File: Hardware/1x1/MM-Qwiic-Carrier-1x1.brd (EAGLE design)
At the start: 80 x 34.3 mm, 63 parts, among them J15 MICROMOD-2222-C, J2 QWIIC_RIGHT_ANGLE, U1 MCP73831, U5 AP7361C-33FGEUDFN-8

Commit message: Remove production files. Design review changes
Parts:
- removed H6, H7, H8, H9: STAND-OFF-REFLOW2.5MM_TALL, SparkFun-Hardware:STAND-OFF-REFLOW-M2.5
- removed JP1: JUMPER-SMT_2_NC_TRACE_SILK, SparkFun-Jumpers:SMT-JUMPER_2_NC_TRACE_SILK
- added D5: 3A/10V/280mV, SparkFun-DiscreteSemi:SOD-323
- added J4: (no value), SparkFun-Connectors:1X02_NO_SILK
- added J5: Vertical Qwiic Connector, SparkFun-Connectors:JST04_1MM_VERT
- added J6: (no value), SparkFun-Connectors:1X08_NO_SILK
- added TP1, TP2: TEST-POINT3X5, SparkFun-Connectors:PAD.03X.05
- U$5: value (none) -> QWIIC_BOARD_OUTLINESTANDOFF; device output:#VIN#0 -> SparkFun-Boards:QWIIC_BOARD_MOUNT_SMD_STANDOFFS
- moved U$5 47.9 mm to (62.2, 17.8), flipped to the top
- moved U$3 41.5 mm to (91.8, 10.7)
- moved LOGO2 27.9 mm to (33.4, 3.11)
- moved J2 27.9 mm to (38.1, 5.08)
- moved U$4 17.4 mm to (5.84, 31.8)
- moved D4 17.3 mm to (11.4, 31.8)
- moved JP4 15.1 mm to (15.2, 33.7)
- moved R11 15.1 mm to (15.2, 33.7)
- moved U$6 15.1 mm to (21.0, 33.5)
- moved R4 11.9 mm to (15.0, 29.2)
- moved D2 11.3 mm to (11.4, 33.7), turned to 180 degrees
- moved U$19 10.5 mm to (15.9, 0.76), turned to 90 degrees
- moved U$2 10.4 mm to (6.99, 0.51), turned to 90 degrees
- moved C3 8.38 mm to (13.0, 29.2)
- moved J3 8.13 mm to (3.81, 25.4), turned to 90 degrees
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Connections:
- removed net 5V: C4.1, D3.C, D4.A, JP1.2, U1.4
- removed net I2C_SCL: J15.14, J2.4
- removed net I2C_SDA: J15.12, J2.3
- removed net N$5: C3.1, D3.A, J3.2, U1.3
- new net D0: J15.10, J6.3
- new net D1: J15.18, J6.4
- new net I2C_!INT!: J15.16, J6.2
- new net SCL: J15.14, J2.4, J5.4, TP2.P$1
- new net SDA: J15.12, J2.3, J5.3, TP1.P$1
- new net SPI_!CS!: J15.55, J6.8
- new net SPI_CIPO: J15.61, J6.5
- new net SPI_COPI: J15.59, J6.6
- new net SPI_SCK: J15.57, J6.7
- new net V_BATT: C3.1, D3.A, J3.2, J4.1, U1.3
- net 3.3V: now also J5.2
- net GND: now also J4.2, J5.1, J6.1; no longer H6.1, H7.1, H8.1, H9.1
- net N$3: now also D4.C; no longer U1.1
- net N$8: now also U1.1; no longer D4.C
- net VIN: now also D3.C, D5.C; no longer JP1.1
- net V_USB: now also C4.1, D4.A, D5.A, U1.4
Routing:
- net SPI_!CS!: track 0.00 -> 34.9 mm, vias 0 -> 1
- net SPI_SCK: track 0.00 -> 32.4 mm, vias 0 -> 1
- net SPI_COPI: track 0.00 -> 29.3 mm, vias 0 -> 1
- net SDA: track 0.00 -> 28.3 mm, vias 0 -> 2
- net SCL: track 0.00 -> 27.4 mm
- net D0: track 0.00 -> 27.1 mm, vias 0 -> 2
- net D1: track 0.00 -> 27.1 mm
- net SPI_CIPO: track 0.00 -> 26.4 mm, vias 0 -> 1
- net I2C_!INT!: track 0.00 -> 26.2 mm
- net V_USB: track 18.2 -> 44.3 mm, vias 1 -> 3
- net V_BATT: track 0.00 -> 21.7 mm, vias 0 -> 1
- net I2C_SDA: track 20.7 -> 0.00 mm, vias 2 -> 0
- net I2C_SCL: track 20.0 -> 0.00 mm, vias 2 -> 0
- net N$5: track 12.7 -> 0.00 mm
- net 5V: track 12.2 -> 0.00 mm, vias 1 -> 0
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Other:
- board size 80 x 34.3 mm -> 80 x 35.6 mm
- board text added: "in"

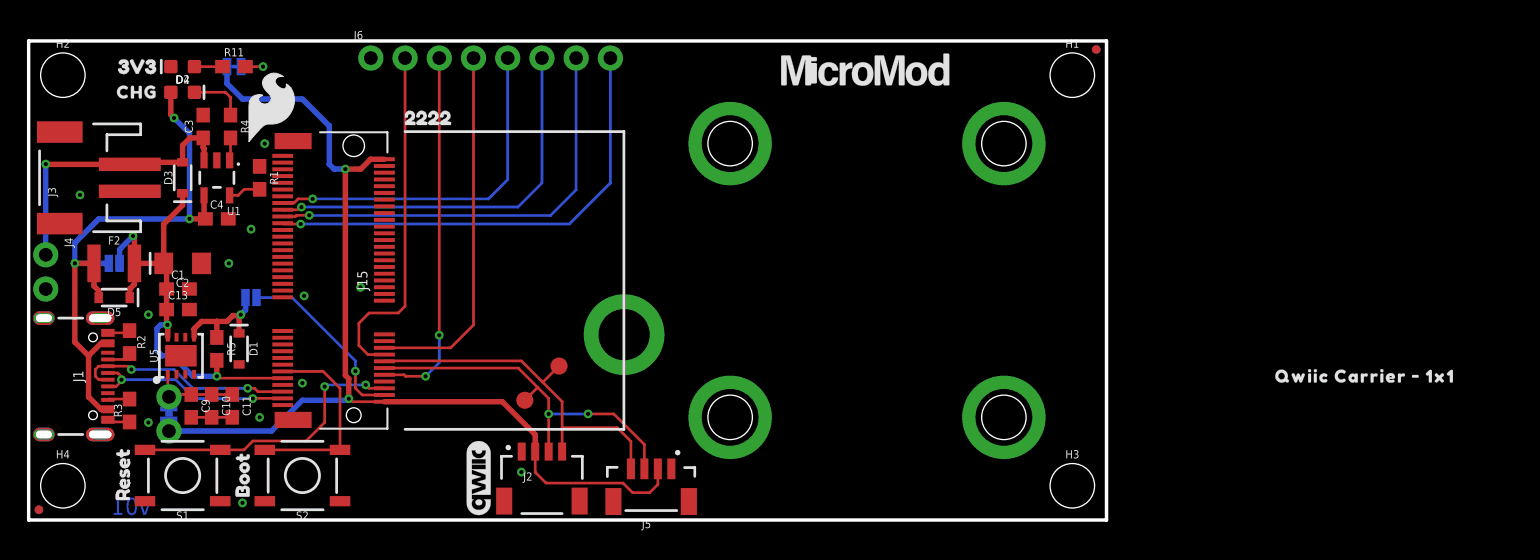
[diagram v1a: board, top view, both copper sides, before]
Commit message: Fix silk screen
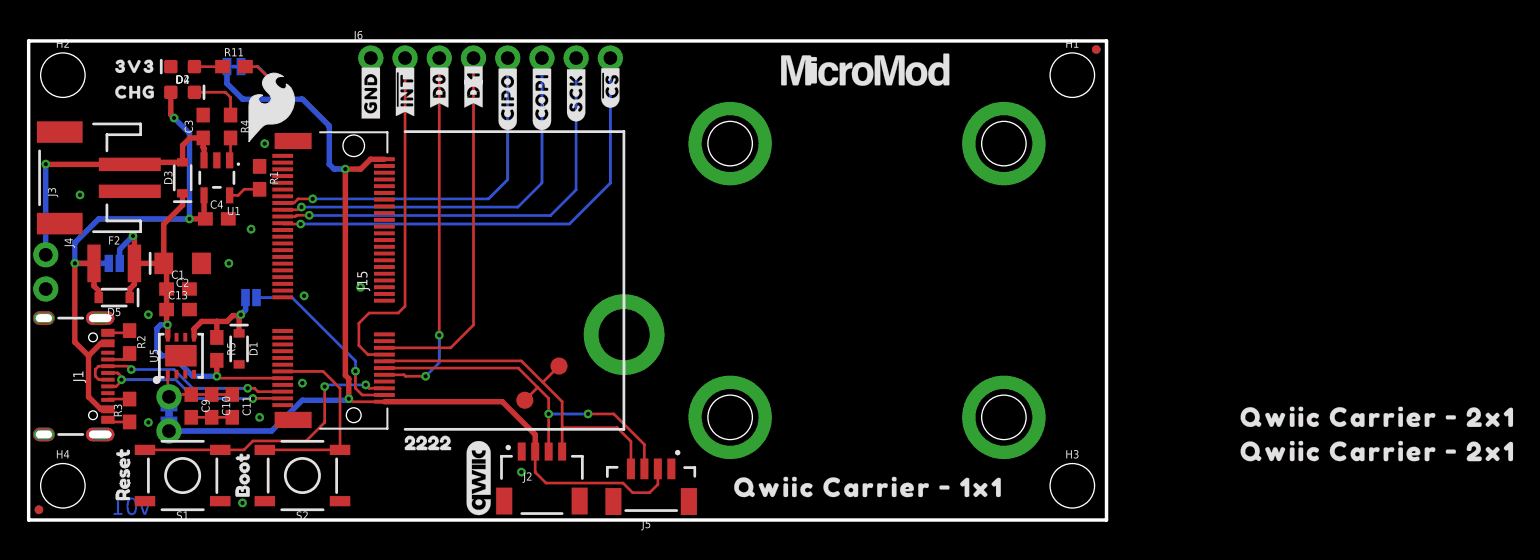
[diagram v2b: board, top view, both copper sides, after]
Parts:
- added U$10, U$13: (no value), output:QWIIC_CARRIER_#_1X10
- added U$11, U$12: (no value), output:QWIIC_CARRIER_#_2X10
- added U$14: (no value), output:#GND#0
- added U$15, U$16: (no value), output:##INT##0
- added U$17, U$18: (no value), output:#D0#0
- added U$20, U$21: (no value), output:#D#0
- added U$22, U$23: (no value), output:#CIPO#0
- added U$24, U$25: (no value), output:#COPI#0
- added U$26, U$27: (no value), output:#SCK#0
- added U$28, U$29: (no value), output:##CS##0
- added U$30, U$31: (no value), output:#1#0
- U$1: device buzzard_labels (5):3V31 -> output:#3#3V_EN#0
- U$3: device output:QWIIC_CARRIER_#_1X1_0 -> output:3V30
- U$8: device output:#VE#0 -> output:#GND#0
- moved U$3 89.1 mm to (5.71, 33.7)
- moved U$55 24.1 mm to (27.0, 5.72)
- moved U$1 19.9 mm to (15.7, 16.5), flipped to the bottom
- moved U$8 16.2 mm to (25.4, 29.5), flipped to the top, turned to 90 degrees
- moved U$68 3.81 mm to (31.8, 19.1)
- moved LOGO1 2.54 mm to (31.8, 21.6)
- moved LOGO3 1.27 mm to (31.6, 10.9)
- moved U$4 0.13 mm to (5.71, 31.8)
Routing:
- net N$4: track 2.95 -> 5.24 mm
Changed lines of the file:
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@@
 <?xml version="1.0" encoding="utf-8"?>
 <!DOCTYPE eagle SYSTEM "eagle.dtd">
-<eagle version="9.5.2">
+<eagle version="9.6.2">
 <drawing>
 <settings>
@@
 <element name="U$19" library="buzzard_labels (10)" package="BOOT2" value="" x="15.875" y="0.762" smashed="yes" rot="R90"/>
 <element name="LOGO2" library="SparkFun-Aesthetics" package="QWIIC_5.5MM" value="QWIIC_LOGO_CONNECTOR" x="33.401" y="3.1115" smashed="yes" rot="R90"/>
-<element name="LOGO3" library="SparkFun-Aesthetics" package="OSHW-LOGO-M" value="OSHW-LOGOM" x="31.623" y="9.652" smashed="yes" rot="MR0"/>
-<element name="U$55" library="buzzard_labels (9)" package="22229" value="" x="26.962" y="29.85" smashed="yes"/>
+<element name="LOGO3" library="SparkFun-Aesthetics" package="OSHW-LOGO-M" value="OSHW-LOGOM" x="31.623" y="10.922" smashed="yes" rot="MR0"/>
+<element name="U$55" library="buzzard_labels (9)" package="22229" value="" x="26.962" y="5.72" smashed="yes"/>
 <element name="H5" library="SparkFun-Hardware" package="STAND-OFF-REFLOW-M2.5" value="STAND-OFF-REFLOW2.5MM_TALL" x="44.2" y="13.76" smashed="yes">
 <attribute name="PROD_ID" value="HW-14899" x="44.2" y="13.76" size="1.778" layer="27" font="vector" ratio="15" display="off"/>
@@
 <attribute name="VALUE" x="23.495" y="17.78" size="0.762" layer="27" rot="R270" align="center"/>
 </element>
-<element name="LOGO1" library="SparkFun-Aesthetics" package="SFE_LOGO_NAME_FLAME_.2" value="SFE_LOGO_NAME_FLAME.2_INCH" x="31.75" y="19.05" smashed="yes" rot="MR0"/>
-<element name="U$1" library="buzzard_labels (5)" package="3V31" value="" x="5.715" y="33.655" smashed="yes"/>
+<element name="LOGO1" library="SparkFun-Aesthetics" package="SFE_LOGO_NAME_FLAME_.2" value="SFE_LOGO_NAME_FLAME.2_INCH" x="31.75" y="21.59" smashed="yes" rot="MR0"/>
 <element name="U$44" library="SparkFun-Aesthetics" package="SFE_LOGO_FLAME_.2" value="" x="18.034" y="30.607" smashed="yes"/>
 <element name="U$67" library="SparkFun-MicroMod" package="MICROMOD_LOGO_.5" value="" x="62.103" y="33.401" smashed="yes"/>
-<element name="U$68" library="SparkFun-MicroMod" package="MICROMOD_LOGO_.5" value="" x="31.75" y="15.24" smashed="yes" rot="MR0"/>
+<element name="U$68" library="SparkFun-MicroMod" package="MICROMOD_LOGO_.5" value="" x="31.75" y="19.05" smashed="yes" rot="MR0"/>
 <element name="J2" library="SparkFun-Connectors" package="JST04_1MM_RA" value="QWIIC_RIGHT_ANGLE" x="38.1" y="5.08" smashed="yes">
 <attribute name="NAME" x="36.703" y="2.921" size="0.6096" layer="25" font="vector" ratio="20"/>
@@
 <attribute name="VALUE" x="14.224" y="29.21" size="0.6096" layer="27" font="vector" ratio="20" rot="R270" align="top-center"/>
 </element>
-<element name="U$3" library="output" package="QWIIC_CARRIER_#_1X1_0" value="" x="91.821" y="10.668" smashed="yes"/>
-<element name="U$4" library="output" package="CHG0" value="" x="5.842" y="31.75" smashed="yes"/>
+<element name="U$4" library="output" package="CHG0" value="" x="5.715" y="31.75" smashed="yes"/>
 <element name="U$6" library="output" package="#3#3V#0" value="" x="20.955" y="33.528" smashed="yes" rot="MR0"/>
 <element name="U$7" library="output" package="#BYP#0" value="" x="11.43" y="19.05" smashed="yes" rot="MR0"/>
 <element name="U$9" library="output" package="#MEAS#0" value="" x="16.51" y="7.874" smashed="yes" rot="MR0"/>
-<element name="U$8" library="output" package="#VE#0" value="" x="15.748" y="16.51" smashed="yes" rot="MR0"/>
 <element name="TP1" library="SparkFun-Connectors" package="PAD.03X.05" value="TEST-POINT3X5" x="36.83" y="8.89" smashed="yes"/>
 <element name="TP2" library="SparkFun-Connectors" package="PAD.03X.05" value="TEST-POINT3X5" x="39.37" y="11.43" smashed="yes"/>
@@
 </element>
 <element name="U$5" library="SparkFun-Boards" package="QWIIC_BOARD_MOUNT_SMD_STANDOFFS" value="QWIIC_BOARD_OUTLINESTANDOFF" x="62.23" y="17.78" smashed="yes"/>
+<element name="U$10" library="output" package="QWIIC_CARRIER_#_1X10" value="" x="51.308" y="2.413" smashed="yes"/>
+<element name="U$11" library="output" package="QWIIC_CARRIER_#_2X10" value="" x="88.9" y="7.62" smashed="yes"/>
+<element name="U$12" library="output" package="QWIIC_CARRIER_#_2X10" value="" x="88.9" y="5.08" smashed="yes"/>
+<element name="U$13" library="output" package="QWIIC_CARRIER_#_1X10" value="" x="42.672" y="16.637" smashed="yes" rot="MR0"/>
+<element name="U$3" library="output" package="3V30" value="" x="5.715" y="33.655" smashed="yes"/>
+<element name="U$1" library="output" package="#3#3V_EN#0" value="" x="15.748" y="16.51" smashed="yes" rot="MR0"/>
+<element name="U$8" library="output" package="#GND#0" value="" x="25.4" y="29.464" smashed="yes" rot="R90"/>
+<element name="U$14" library="output" package="#GND#0" value="" x="25.4" y="29.464" smashed="yes" rot="MR90"/>
+<element name="U$15" library="output" package="##INT##0" value="" x="27.94" y="29.972" smashed="yes" rot="R90"/>
+<element name="U$16" library="output" package="##INT##0" value="" x="27.94" y="29.972" smashed="yes" rot="MR90"/>
+<element name="U$17" library="output" package="#D0#0" value="" x="30.48" y="30.607" smashed="yes" rot="R90"/>
+<element name="U$18" library="output" package="#D0#0" value="" x="30.48" y="30.607" smashed="yes" rot="MR90"/>
+<element name="U$22" library="output" package="#CIPO#0" value="" x="35.56" y="28.956" smashed="yes" rot="R90"/>
+<element name="U$23" library="output" package="#CIPO#0" value="" x="35.56" y="28.956" smashed="yes" rot="MR90"/>
+<element name="U$24" library="output" package="#COPI#0" value="" x="38.1" y="28.956" smashed="yes" rot="R90"/>
+<element name="U$25" library="output" package="#COPI#0" value="" x="38.1" y="28.956" smashed="yes" rot="MR90"/>
+<element name="U$26" library="output" package="#SCK#0" value="" x="40.64" y="29.591" smashed="yes" rot="R90"/>
+<element name="U$27" library="output" package="#SCK#0" value="" x="40.64" y="29.591" smashed="yes" rot="MR90"/>
+<element name="U$28" library="output" package="##CS##0" value="" x="43.18" y="30.607" smashed="yes" rot="R90"/>
+<element name="U$29" library="output" package="##CS##0" value="" x="43.18" y="30.607" smashed="yes" rot="MR90"/>
+<element name="U$20" library="output" package="#D#0" value="" x="33.02" y="30.607" smashed="yes" rot="R90"/>
+<element name="U$21" library="output" package="#D#0" value="" x="33.02" y="30.607" smashed="yes" rot="MR90"/>
+<element name="U$30" library="output" package="#1#0" value="" x="33.02" y="32.004" smashed="yes" rot="R90"/>
+<element name="U$31" library="output" package="#1#0" value="" x="33.02" y="32.004" smashed="yes" rot="MR90"/>
 </elements>
 <signals>
@@
 <contactref element="R11" pad="2"/>
 <contactref element="JP4" pad="1"/>
-<wire x1="16.09" y1="33.655" x2="17.399" y2="33.655" width="0.2032" layer="1"/>
-<via x="17.399" y="33.655" extent="1-16" drill="0.3048"/>
-<wire x1="17.399" y1="33.655" x2="15.7607" y2="33.655" width="0.2032" layer="16"/>
+<wire x1="17.653" y1="32.385" x2="17.653" y2="32.981" width="0.2032" layer="1"/>
+<wire x1="17.653" y1="32.981" x2="16.979" y2="33.655" width="0.2032" layer="1"/>
+<wire x1="16.09" y1="33.655" x2="16.979" y2="33.655" width="0.2032" layer="1"/>
+<via x="17.653" y="32.385" extent="1-16" drill="0.3048"/>
+<wire x1="17.653" y1="32.385" x2="17.653" y2="33.0327" width="0.2032" layer="16"/>
+<wire x1="17.653" y1="33.0327" x2="17.0307" y2="33.655" width="0.2032" layer="16"/>
+<wire x1="17.0307" y1="33.655" x2="15.7607" y2="33.655" width="0.2032" layer="16"/>
 </signal>
 <signal name="N$6">

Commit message: Checklist
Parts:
- removed U$11, U$12: (no value), output:QWIIC_CARRIER_#_2X10
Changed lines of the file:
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@@
 <?xml version="1.0" encoding="utf-8"?>
 <!DOCTYPE eagle SYSTEM "eagle.dtd">
-<eagle version="9.6.2">
+<eagle version="9.5.2">
 <drawing>
 <settings>
-<setting alwaysvectorfont="yes"/>
+<setting alwaysvectorfont="no"/>
 <setting verticaltext="up"/>
 </settings>
@@
 <layer number="37" name="tTest" color="7" fill="1" visible="no" active="yes"/>
 <layer number="38" name="bTest" color="7" fill="1" visible="no" active="yes"/>
-<layer number="39" name="tKeepout" color="4" fill="11" visible="yes" active="yes"/>
+<layer number="39" name="tKeepout" color="4" fill="11" visible="no" active="yes"/>
 <layer number="40" name="bKeepout" color="1" fill="11" visible="no" active="yes"/>
 <layer number="41" name="tRestrict" color="4" fill="10" visible="no" active="yes"/>
@@
 <text x="43.434" y="39.878" size="1.778" layer="47" font="vector" ratio="15">in</text>
 <text x="81.534" y="23.241" size="1.778" layer="47" font="vector" ratio="15" rot="R270">in</text>
+<dimension x1="2.54" y1="33.02" x2="77.47" y2="33.02" x3="40.005" y3="44.45" textsize="1.778" textratio="15" layer="47" unit="inch"/>
+<dimension x1="77.47" y1="33.02" x2="77.47" y2="2.54" x3="88.9" y3="17.78" textsize="1.778" textratio="15" layer="47" unit="inch"/>
+<text x="43.434" y="44.958" size="1.778" layer="47" font="vector" ratio="15">in</text>
+<text x="86.614" y="23.241" size="1.778" layer="47" font="vector" ratio="15" rot="R270">in</text>
 </plain>
 <attributes>
@@
 <element name="U$5" library="SparkFun-Boards" package="QWIIC_BOARD_MOUNT_SMD_STANDOFFS" value="QWIIC_BOARD_OUTLINESTANDOFF" x="62.23" y="17.78" smashed="yes"/>
 <element name="U$10" library="output" package="QWIIC_CARRIER_#_1X10" value="" x="51.308" y="2.413" smashed="yes"/>
-<element name="U$11" library="output" package="QWIIC_CARRIER_#_2X10" value="" x="88.9" y="7.62" smashed="yes"/>
-<element name="U$12" library="output" package="QWIIC_CARRIER_#_2X10" value="" x="88.9" y="5.08" smashed="yes"/>
 <element name="U$13" library="output" package="QWIIC_CARRIER_#_1X10" value="" x="42.672" y="16.637" smashed="yes" rot="MR0"/>
 <element name="U$3" library="output" package="3V30" value="" x="5.715" y="33.655" smashed="yes"/>

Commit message: silkscreen
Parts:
- added U$11, U$32: (no value), output:#0
- added U$12: (no value), output:#VBAT#0
- added U$33: (no value), output:#GND#0
- added U$36, U$37: (no value), buzzard_labels (1):#0
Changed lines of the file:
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@@
 <?xml version="1.0" encoding="utf-8"?>
 <!DOCTYPE eagle SYSTEM "eagle.dtd">
-<eagle version="9.5.2">
+<eagle version="9.6.2">
 <drawing>
 <settings>
@@
 <element name="U$30" library="output" package="#1#0" value="" x="33.02" y="32.004" smashed="yes" rot="R90"/>
 <element name="U$31" library="output" package="#1#0" value="" x="33.02" y="32.004" smashed="yes" rot="MR90"/>
+<element name="U$12" library="output" package="#VBAT#0" value="" x="7.366" y="19.685" smashed="yes" rot="MR0"/>
+<element name="U$33" library="output" package="#GND#0" value="" x="6.096" y="17.145" smashed="yes" rot="MR0"/>
+<element name="U$11" library="output" package="#0" value="" x="1.524" y="19.685" smashed="yes"/>
+<element name="U$32" library="output" package="#0" value="" x="7.747" y="27.813" smashed="yes"/>
+<element name="U$36" library="buzzard_labels (1)" package="#0" value="" x="1.143" y="17.399" smashed="yes"/>
+<element name="U$37" library="buzzard_labels (1)" package="#0" value="" x="7.366" y="23.495" smashed="yes"/>
 </elements>
 <signals>

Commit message: Review before ordering
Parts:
- moved U$2 3.81 mm to (10.8, 0.38)
- moved S1 3.81 mm to (15.2, 3.30)
- moved S2 3.81 mm to (24.1, 3.30)
- moved U$19 3.81 mm to (19.7, 0.76)
- moved TP2 1.27 mm to (39.4, 12.7), flipped to the bottom
- moved C11 0.25 mm to (15.4, 8.47)
- moved C9 0.25 mm to (12.3, 8.47)
- moved C10 0.25 mm to (13.8, 8.47)
- flipped TP1 to the bottom
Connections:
- new net V_USB_2: BYP.1, D5.C, F2.1
- net VIN: no longer D5.C
- net V_USB: no longer BYP.1, F2.1
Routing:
- net V_USB_2: track 0.00 -> 9.63 mm, vias 0 -> 1
- net V_USB: track 44.3 -> 39.5 mm
- net !RESET!: track 21.4 -> 17.6 mm
- net VIN: track 34.7 -> 32.0 mm
- net I2C_!INT!: track 26.2 -> 27.9 mm
- net SCL: track 27.4 -> 28.3 mm, vias 0 -> 1
- net SDA: track 28.3 -> 29.1 mm
- net 3.3V: track 78.7 -> 78.8 mm, vias 2 -> 4
